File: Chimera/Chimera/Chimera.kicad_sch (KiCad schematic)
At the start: 79 parts, among them J1 Fork 1, J2 Fork 2, J3 Flamethrower, J4 Therm 1, J5 Therm 2, J6 Therm 3, J7 Therm 4, SW1 PTS810 SJK 250 SMTR LFS, U1 DRV8244HQRYJRQ1, U2 DRV8244HQRYJRQ1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

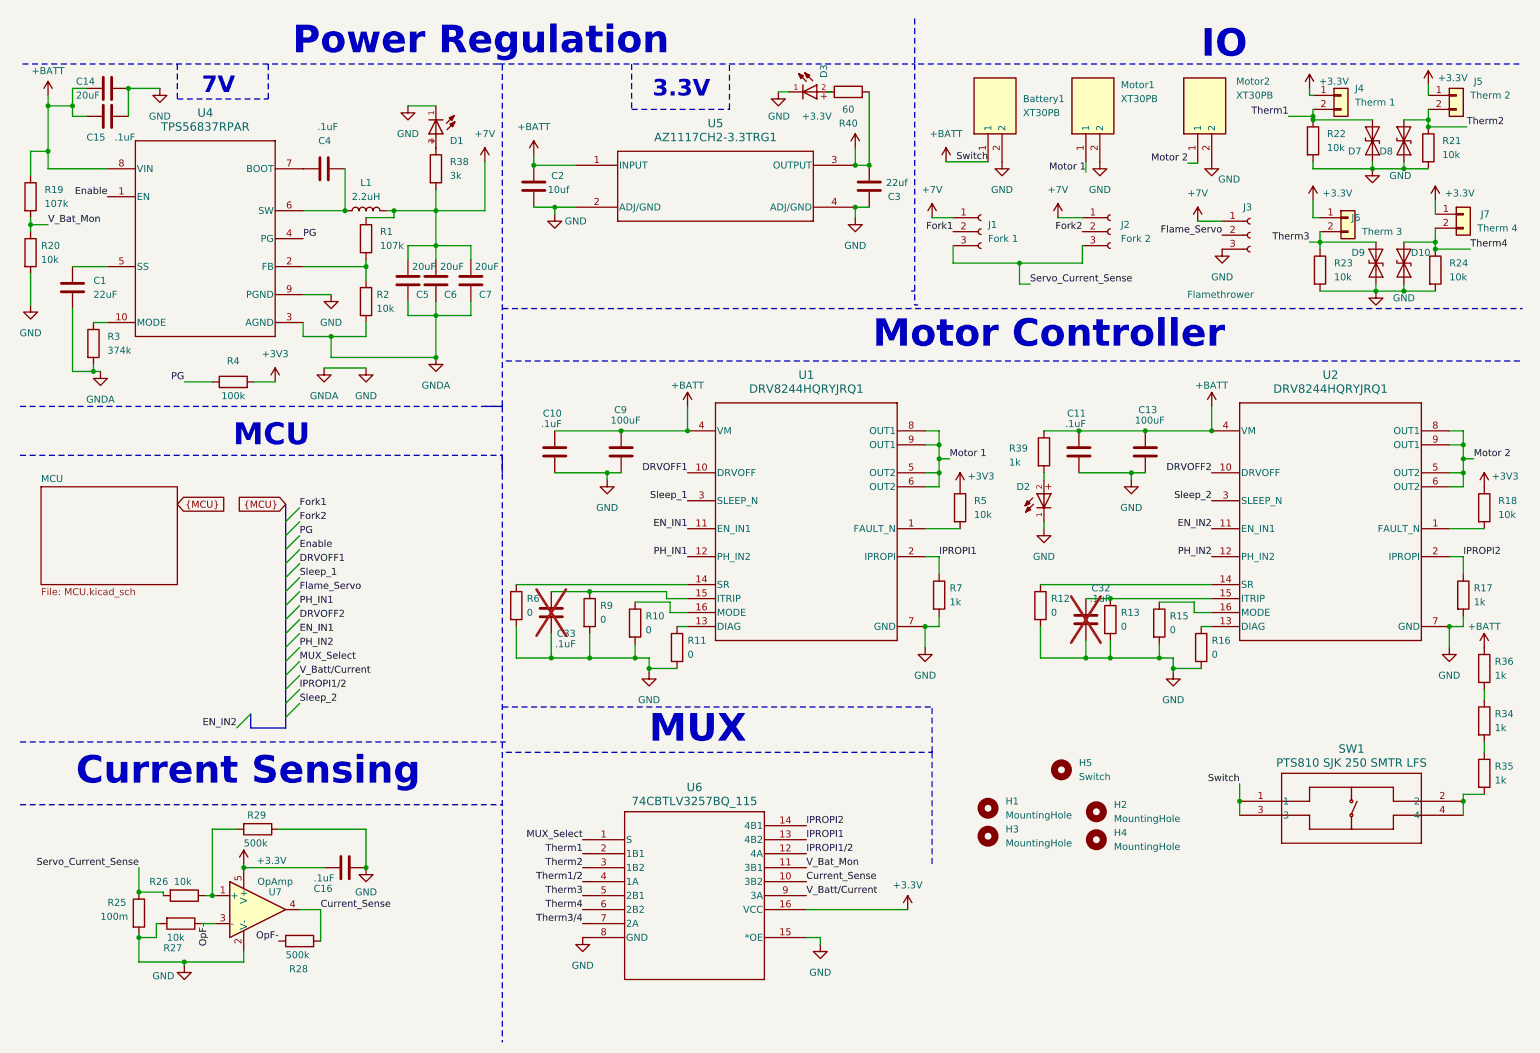
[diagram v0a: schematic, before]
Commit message: Rewiring M2 and moved Debugging LEDS
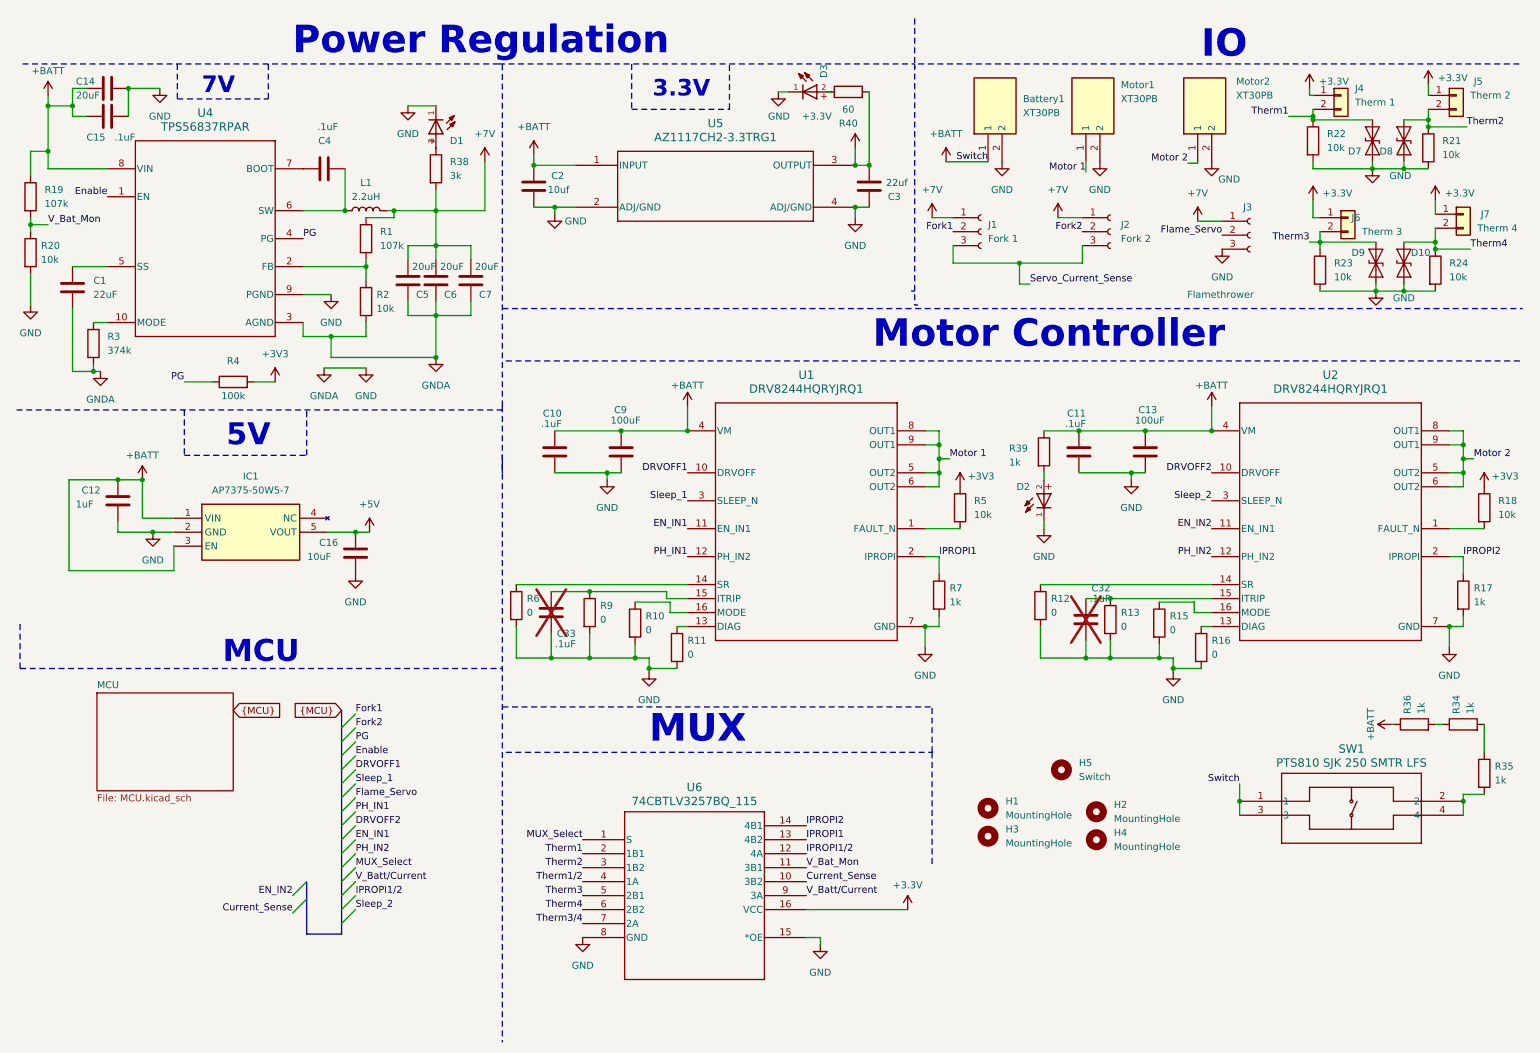
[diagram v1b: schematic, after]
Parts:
- removed R25: 100m, Resistor_SMD:R_0805_2012Metric, symbol Device:R
- removed R26, R27: 10k, Resistor_SMD:R_0805_2012Metric, symbol Device:R
- removed R28, R29: 500k, Resistor_SMD:R_0805_2012Metric, symbol Device:R
- removed U7: OpAmp, chimera:SC70-5_LT_MCH-M, symbol OEM:OpAmp
- added C12: 1uF, Capacitor_SMD:C_0805_2012Metric, symbol Device:C
- added IC1: AP7375-50W5-7, SOT95P285X140-5N, symbol Chimera:AP7375-50W5-7
- C16: value .1uF -> 10uF
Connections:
- net +3.3V: no longer C16.2
- net +BATT: now also C12.2, IC1.1 (VIN), IC1.3 (EN)
- net GND: now also C12.1, IC1.2 (GND)
- new net +5V: C16.2, IC1.5 (VOUT)
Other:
- note added: "5V"
- note removed: "Current Sensing"
- moved on the sheet: R34, R36

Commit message: Saving changes, to revert and look at previous routing
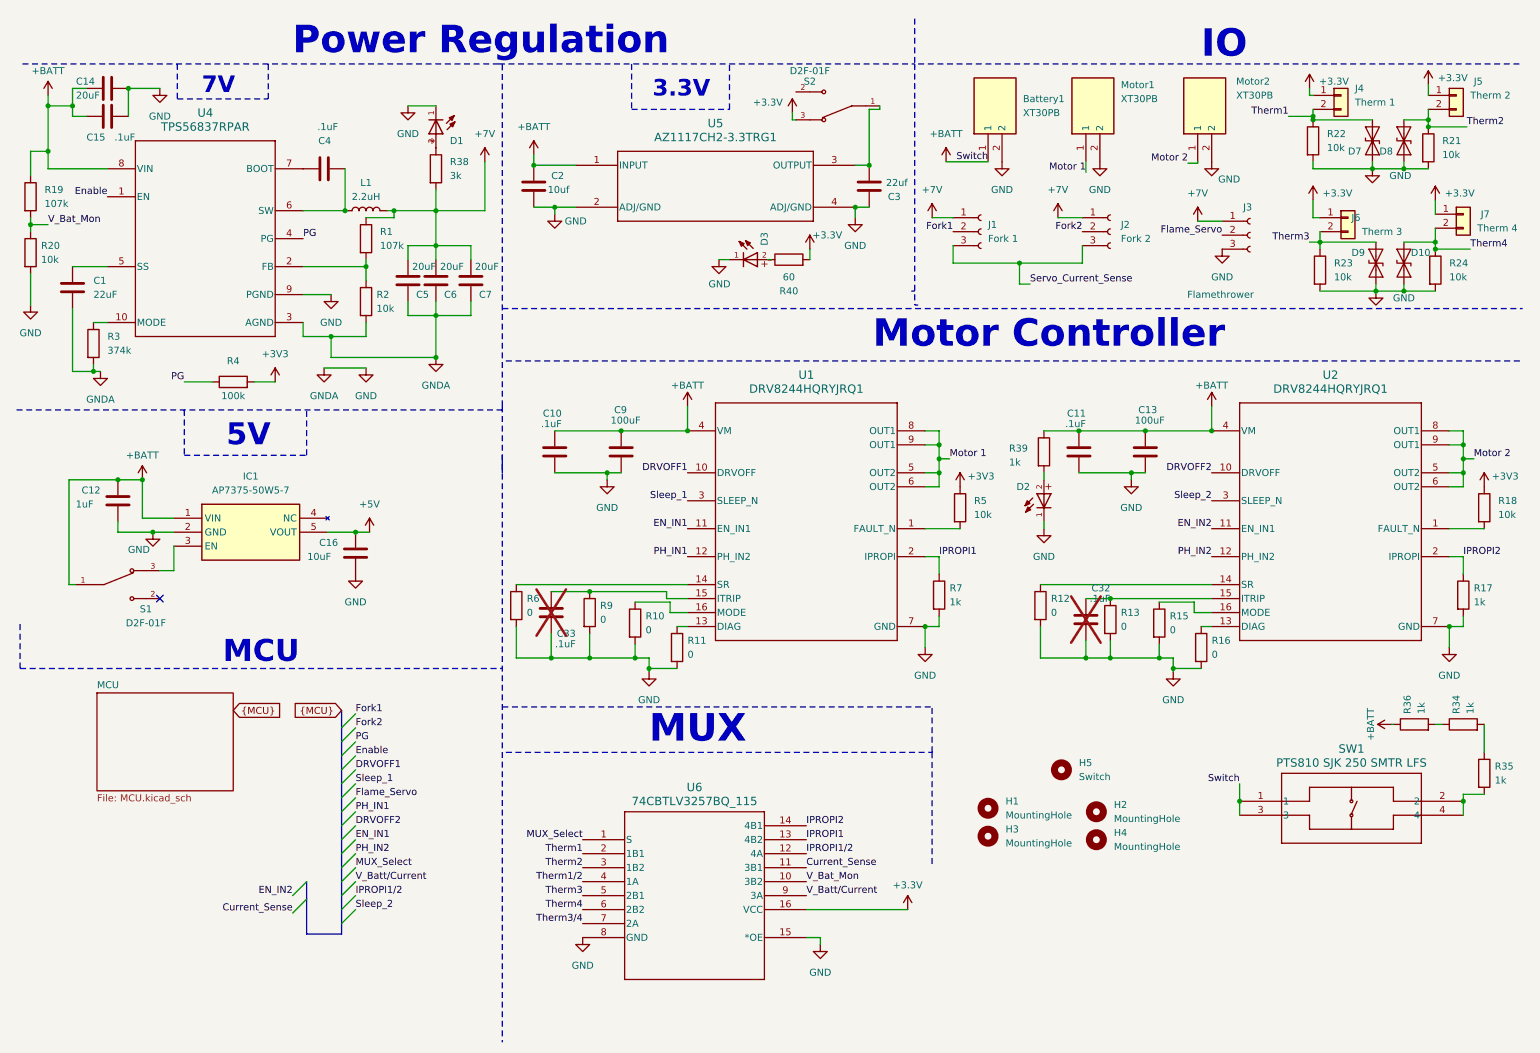
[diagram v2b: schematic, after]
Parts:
- added S1, S2: D2F-01F, SW_D2F-01F, symbol Chimera:D2F-01F
- U4: footprint chimera:RPA0010A-MFG -> chimera:CONV_TPS56837RPAR
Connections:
- net +3.3V: now also S2.3; no longer C3.2, U5.3 (OUTPUT)
- net +BATT: now also S1.1; no longer IC1.3 (EN)
- net Current_Sense: now also U6.11 (3B1); no longer U6.10 (3B2)
- net V_Bat_Mon: now also U6.10 (3B2); no longer U6.11 (3B1)
- new net: IC1.3 (EN), S1.3
- new net: C3.2, S2.1, U5.3 (OUTPUT)
- no-connect marks 0 -> 1
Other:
- moved on the sheet: D3, R40

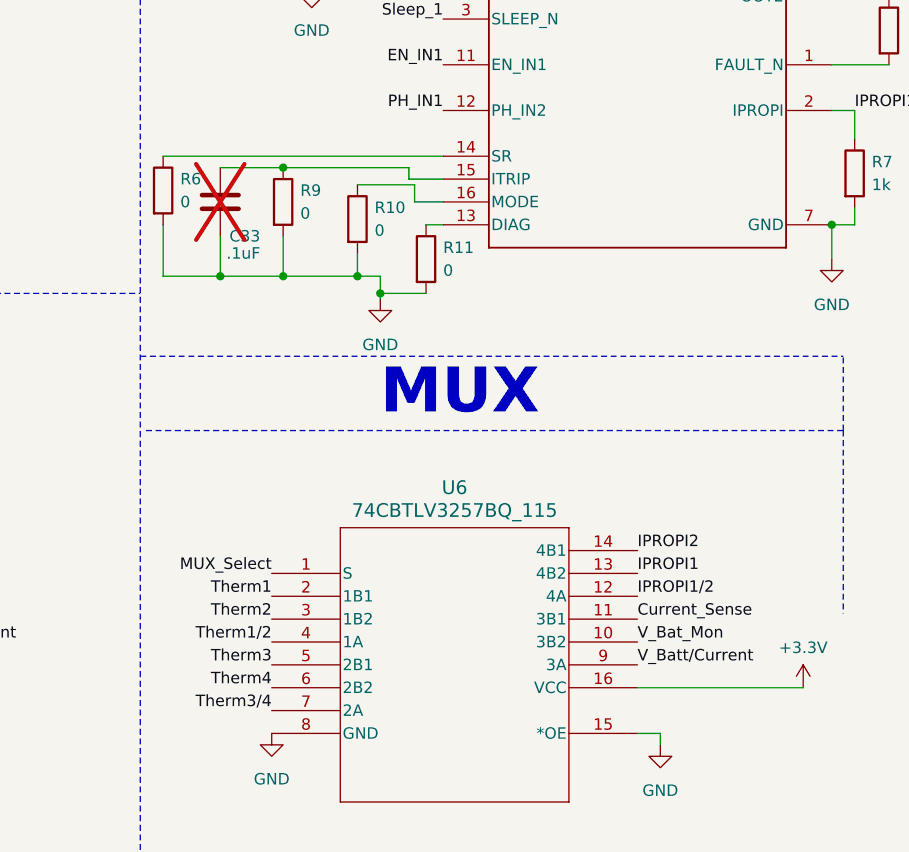
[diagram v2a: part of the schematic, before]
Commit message: Finalized MUX and thermistor wiring, Need to revise Buck and add Opamp surronding circuitry
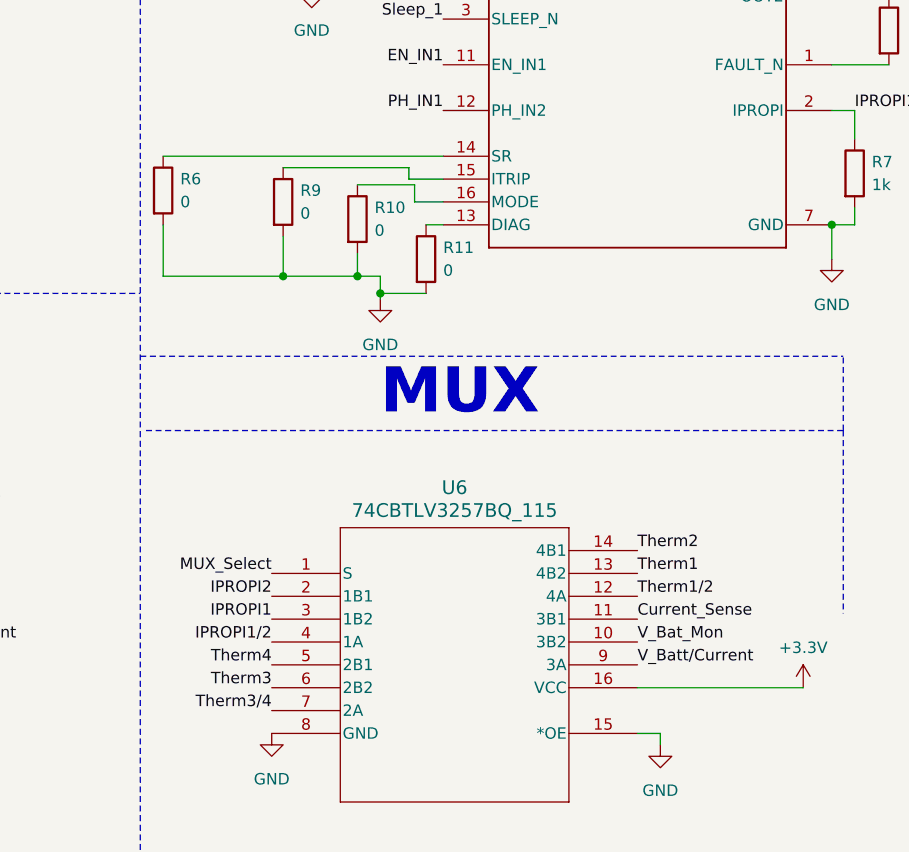
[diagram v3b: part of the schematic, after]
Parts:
- removed C33: .1uF, Capacitor_SMD:C_0805_2012Metric, symbol Device:C
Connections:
- net IPROPI1: now also U6.3 (1B2); no longer U6.13 (4B2)
- net IPROPI1/2: now also U6.4 (1A); no longer U6.12 (4A)
- net IPROPI2: now also U6.2 (1B1); no longer U6.14 (4B1)
- net Therm1: now also U6.13 (4B2); no longer U6.2 (1B1)
- net Therm1/2: now also U6.12 (4A); no longer U6.4 (1A)
- net Therm2: now also U6.14 (4B1); no longer U6.3 (1B2)
- net Therm3: now also U6.6 (2B2); no longer U6.5 (2B1)
- net Therm4: now also U6.5 (2B1); no longer U6.6 (2B2)
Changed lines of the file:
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@@
   (junction (at 17.145 36.195) (diameter 0) (color 0 0 0 0)
   )
-  (junction (at 115.57 116.205) (diameter 0) (color 0 0 0 0)
-  )
   (junction (at 193.675 56.515) (diameter 0) (color 0 0 0 0)
   )
@@
   (junction (at 257.81 39.37) (diameter 0) (color 0 0 0 0)
   )
-  (junction (at 108.585 128.27) (diameter 0) (color 0 0 0 0)
-  )
   (junction (at 87.63 53.34) (diameter 0) (color 0 0 0 0)
   )
@@
     (stroke (width 0) (type default))
   )
-  (wire (pts (xy 102.235 128.27) (xy 108.585 128.27))
+  (wire (pts (xy 102.235 128.27) (xy 115.57 128.27))
     (stroke (width 0) (type default))
   )
@@
     (stroke (width 0) (type default))
   )
-  (wire (pts (xy 108.585 128.27) (xy 115.57 128.27))
-    (stroke (width 0) (type default))
-  )
   (polyline (pts (xy 100.33 145.415) (xy 177.8 145.415))
     (stroke (width 0) (type dash))
@@
     (stroke (width 0) (type default))
   )
-  (wire (pts (xy 108.585 116.205) (xy 115.57 116.205))
-    (stroke (width 0) (type default))
-  )
   (wire (pts (xy 31.75 24.765) (xy 37.465 24.765))
     (stroke (width 0) (type default))
@@
     (stroke (width 0) (type default))
   )
-  (wire (pts (xy 108.585 123.825) (xy 108.585 128.27))
-    (stroke (width 0) (type default))
-  )
   (wire (pts (xy 274.32 92.075) (xy 274.32 94.615))
     (stroke (width 0) (type default))
@@
     (effects (font (size 1.27 1.27)) (justify left bottom))
   )
-  (label "Therm3" (at 114.3 171.45 180) (fields_autoplaced)
+  (label "Therm3" (at 114.3 173.99 180) (fields_autoplaced)
     (effects (font (size 1.27 1.27)) (justify right bottom))
   )
+  (label "V_Batt{slash}Current" (at 154.94 171.45 0) (fields_autoplaced)
+    (effects (font (size 1.27 1.27)) (justify left bottom))
+  )
   (label "EN_IN1" (at 133.35 104.775 180) (fields_autoplaced)
     (effects (font (size 1.27 1.27)) (justify right bottom))
@@
     (effects (font (size 1.27 1.27)) (justify right bottom))
   )
-  (label "V_Batt{slash}Current" (at 154.94 171.45 0) (fields_autoplaced)
+  (label "IPROPI1{slash}2" (at 114.3 168.91 180) (fields_autoplaced)
+    (effects (font (size 1.27 1.27)) (justify right bottom))
+  )
+  (label "IPROPI2" (at 114.3 163.83 180) (fields_autoplaced)
+    (effects (font (size 1.27 1.27)) (justify right bottom))
+  )
+  (label "V_Bat_Mon" (at 154.94 168.91 0) (fields_autoplaced)
     (effects (font (size 1.27 1.27)) (justify left bottom))
   )
@@
     (effects (font (size 1.27 1.27)) (justify left bottom))
   )
-  (label "Therm2" (at 114.3 166.37 180) (fields_autoplaced)
-    (effects (font (size 1.27 1.27)) (justify right bottom))
-  )
   (label "Motor 1" (at 180.975 92.075 0) (fields_autoplaced)
     (effects (font (size 1.27 1.27)) (justify left bottom))
   )
-  (label "V_Bat_Mon" (at 154.94 168.91 0) (fields_autoplaced)
-    (effects (font (size 1.27 1.27)) (justify left bottom))
-  )
   (label "Flame_Servo" (at 230.505 51.435 180) (fields_autoplaced)
     (effects (font (size 1.27 1.27)) (justify right bottom))
@@
     (effects (font (size 1.27 1.27)) (justify left bottom))
   )
+  (label "Therm4" (at 114.3 171.45 180) (fields_autoplaced)
+    (effects (font (size 1.27 1.27)) (justify right bottom))
+  )
   (label "Enable" (at 27.94 44.45 180) (fields_autoplaced)
     (effects (font (size 1.27 1.27)) (justify right bottom))
@@
     (effects (font (size 1.27 1.27)) (justify left bottom))
   )
-  (label "IPROPI1{slash}2" (at 154.94 163.83 0) (fields_autoplaced)
-    (effects (font (size 1.27 1.27)) (justify left bottom))
-  )
   (label "Therm2" (at 274.955 31.75 0) (fields_autoplaced)
     (effects (font (size 1.27 1.27)) (justify left bottom))
@@
     (effects (font (size 1.27 1.27)) (justify right bottom))
   )
-  (label "IPROPI2" (at 154.94 158.75 0) (fields_autoplaced)
-    (effects (font (size 1.27 1.27)) (justify left bottom))
-  )
   (label "Therm3{slash}4" (at 114.3 176.53 180) (fields_autoplaced)
     (effects (font (size 1.27 1.27)) (justify right bottom))
   )
-  (label "Therm4" (at 275.59 53.975 0) (fields_autoplaced)
+  (label "Therm1" (at 154.94 161.29 0) (fields_autoplaced)
     (effects (font (size 1.27 1.27)) (justify left bottom))
   )
-  (label "Current_Sense" (at 154.94 166.37 0) (fields_autoplaced)
+  (label "Therm4" (at 275.59 53.975 0) (fields_autoplaced)
     (effects (font (size 1.27 1.27)) (justify left bottom))
   )
@@
     (effects (font (size 1.27 1.27)) (justify left bottom))
   )
-  (label "IPROPI1" (at 154.94 161.29 0) (fields_autoplaced)
-    (effects (font (size 1.27 1.27)) (justify left bottom))
-  )
   (label "Sleep_2" (at 228.6 99.695 180) (fields_autoplaced)
     (effects (font (size 1.27 1.27)) (justify right bottom))
   )
+  (label "IPROPI1" (at 114.3 166.37 180) (fields_autoplaced)
+    (effects (font (size 1.27 1.27)) (justify right bottom))
+  )
   (label "Flame_Servo" (at 73.025 153.67 0) (fields_autoplaced)
     (effects (font (size 1.27 1.27)) (justify left bottom))
   )
-  (label "Therm1" (at 114.3 163.83 180) (fields_autoplaced)
-    (effects (font (size 1.27 1.27)) (justify right bottom))
+  (label "Therm2" (at 154.94 158.75 0) (fields_autoplaced)
+    (effects (font (size 1.27 1.27)) (justify left bottom))
   )
-  (label "Therm4" (at 114.3 173.99 180) (fields_autoplaced)
-    (effects (font (size 1.27 1.27)) (justify right bottom))
+  (label "Current_Sense" (at 154.94 166.37 0) (fields_autoplaced)
+    (effects (font (size 1.27 1.27)) (justify left bottom))
   )
   (label "MUX_Select" (at 73.025 166.37 0) (fields_autoplaced)
@@
     (effects (font (size 1.27 1.27)) (justify left bottom))
   )
-  (label "DRVOFF2" (at 73.025 158.75 0) (fields_autoplaced)
+  (label "Therm1{slash}2" (at 154.94 163.83 0) (fields_autoplaced)
     (effects (font (size 1.27 1.27)) (justify left bottom))
   )
-  (label "Therm1{slash}2" (at 114.3 168.91 180) (fields_autoplaced)
-    (effects (font (size 1.27 1.27)) (justify right bottom))
+  (label "DRVOFF2" (at 73.025 158.75 0) (fields_autoplaced)
+    (effects (font (size 1.27 1.27)) (justify left bottom))
   )
   (label "Fork2" (at 205.105 50.8 180) (fields_autoplaced)
@@
         )
       )
-    )
-  )
-  (symbol (lib_id "Device:C") (at 108.585 120.015 180) (unit 1)
-    (in_bom yes) (on_board yes) (dnp yes)
-    (property "Reference" "C33" (at 113.03 123.825 0)
-      (effects (font (size 1.27 1.27)) (justify left))
-    )
-    (property "Value" ".1uF" (at 113.03 125.73 0)
-      (effects (font (size 1.27 1.27)) (justify left))
-    )
-    (property "Footprint" "Capacitor_SMD:C_0805_2012Metric" (at 107.6198 116.205 0)
-      (effects (font (size 1.27 1.27)) hide)
-    )
-    (property "Datasheet" "~" (at 108.585 120.015 0)
-      (effects (font (size 1.27 1.27)) hide)
-    )
-    (pin "2")
-    (pin "1")
-    (instances
-      (project "Chimera"
-        (path "/dfd9978a-0f69-4125-9852-5613922ebd2e"
-          (reference "C33") (unit 1)
-        )
-      )
